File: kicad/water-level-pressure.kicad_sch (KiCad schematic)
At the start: 38 parts, among them J1 Conn_01x03, J2 Conn_01x02, J3 Conn_01x02, T1 TestPoint, T10 TestPoint, T11 TestPoint, T12 TestPoint, T13 TestPoint, T14 TestPoint, T15 TestPoint, T16 TestPoint, T17 TestPoint, T18 TestPoint, T19 TestPoint, T2 TestPoint, T20 TestPoint, T21 TestPoint, T22 TestPoint, T23 TestPoint, T24 TestPoint, T25 TestPoint, T26 TestPoint, T27 TestPoint, T28 TestPoint, T29 TestPoint, T3 TestPoint, T30 TestPoint, T4 TestPoint, T5 TestPoint, T6 TestPoint, T7 TestPoint, T8 TestPoint, T9 TestPoint

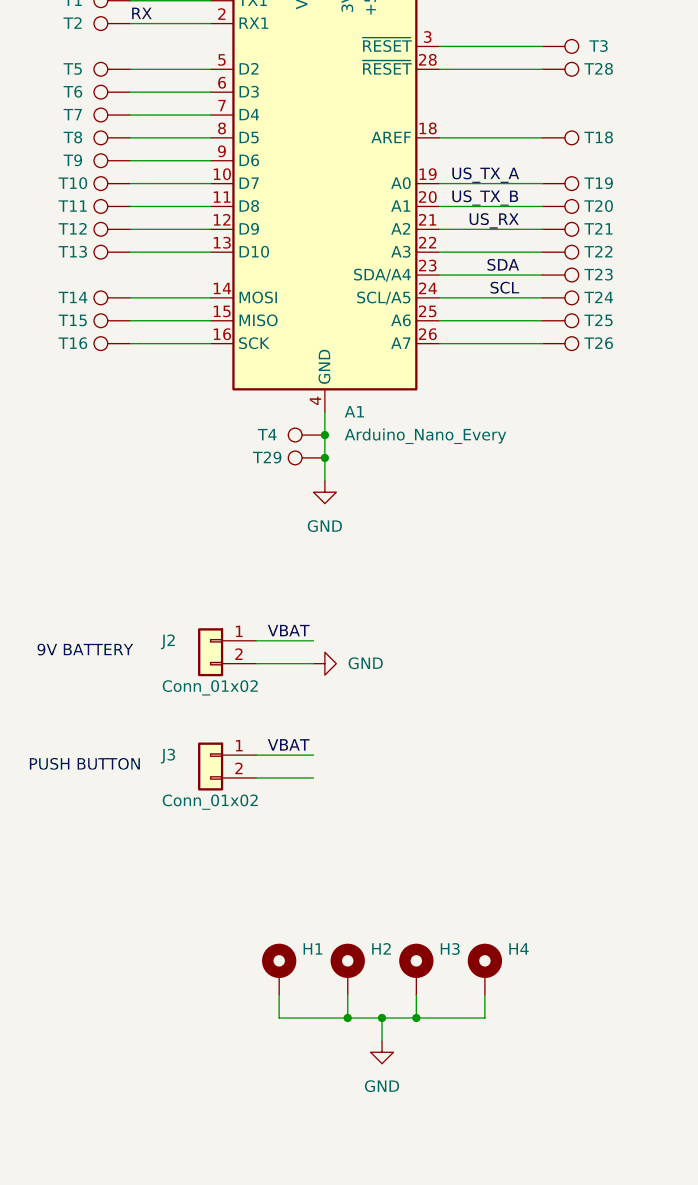
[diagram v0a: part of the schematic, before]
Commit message: Add 9V battery holder.
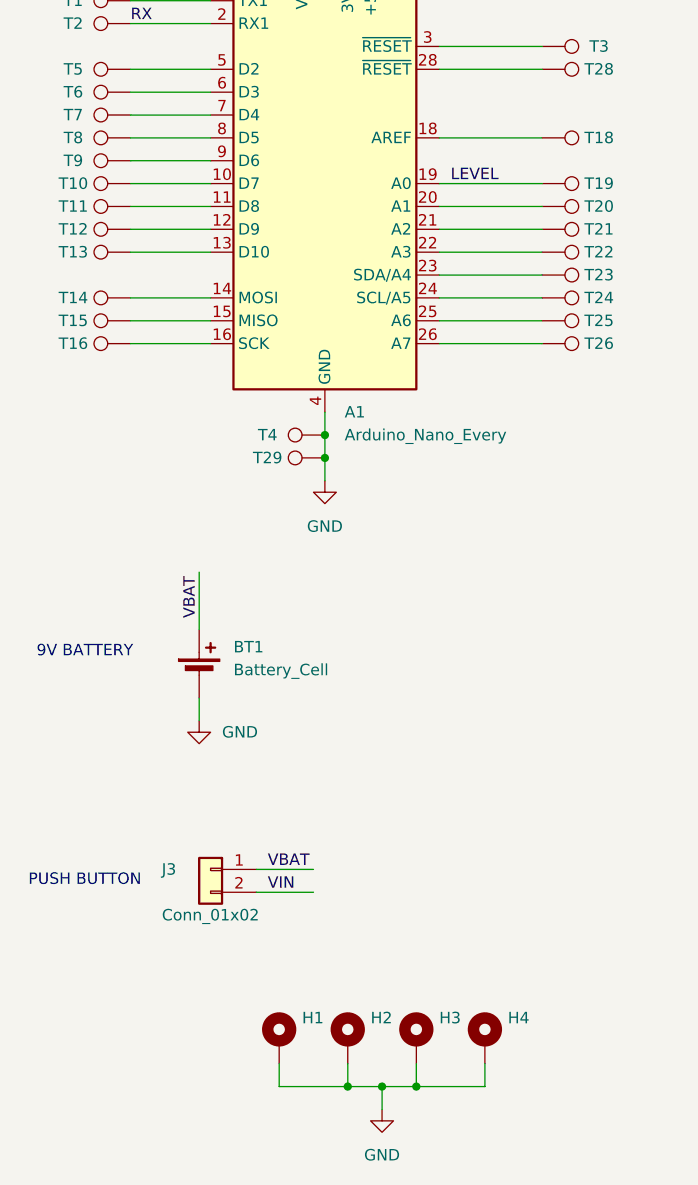
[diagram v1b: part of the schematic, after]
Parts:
- removed J2: Conn_01x02, TerminalBlock_Phoenix:TerminalBlock_Phoenix_MPT-0,5-2-2.54_1x02_P2.54mm_Horizontal, symbol Connector_Generic:Conn_01x02
- added BT1: Battery_Cell, Battery:BatteryHolder_MPD_BA9VPC_1xPP3, symbol Device:Battery_Cell
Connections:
- net US_TX_A is gone; now on net LEVEL: A1.19 (A0), T19.1
- net GND: now also BT1.2 (-)
- net VBAT: now also BT1.1 (+)
- net VIN: now also J3.2 (Pin_2)
- net SCL: no longer names the net of A1.24 (SCL/A5), T24.1
- net SDA: no longer names the net of A1.23 (SDA/A4), T23.1
- net US_RX: no longer names the net of A1.21 (A2), T21.1
- net US_TX_B: no longer names the net of A1.20 (A1), T20.1
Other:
- moved on the sheet: H1, H2, H3, H4, J3
